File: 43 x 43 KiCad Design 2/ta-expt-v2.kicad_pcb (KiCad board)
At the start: 4 copper layers, 43 x 43 mm, 56 parts, among them IC1 BAR43SFILM, IC2 STS5PF30L, IC3 STM32L496VGT3, IC4 IS25LP128F-JBLA3, J1 Conn_01x05, J2 Conn_01x04, J3 USB_C_Receptacle_USB2.0, J4 Conn_01x05, J5 4-174639-8, J6 Conn_01x04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

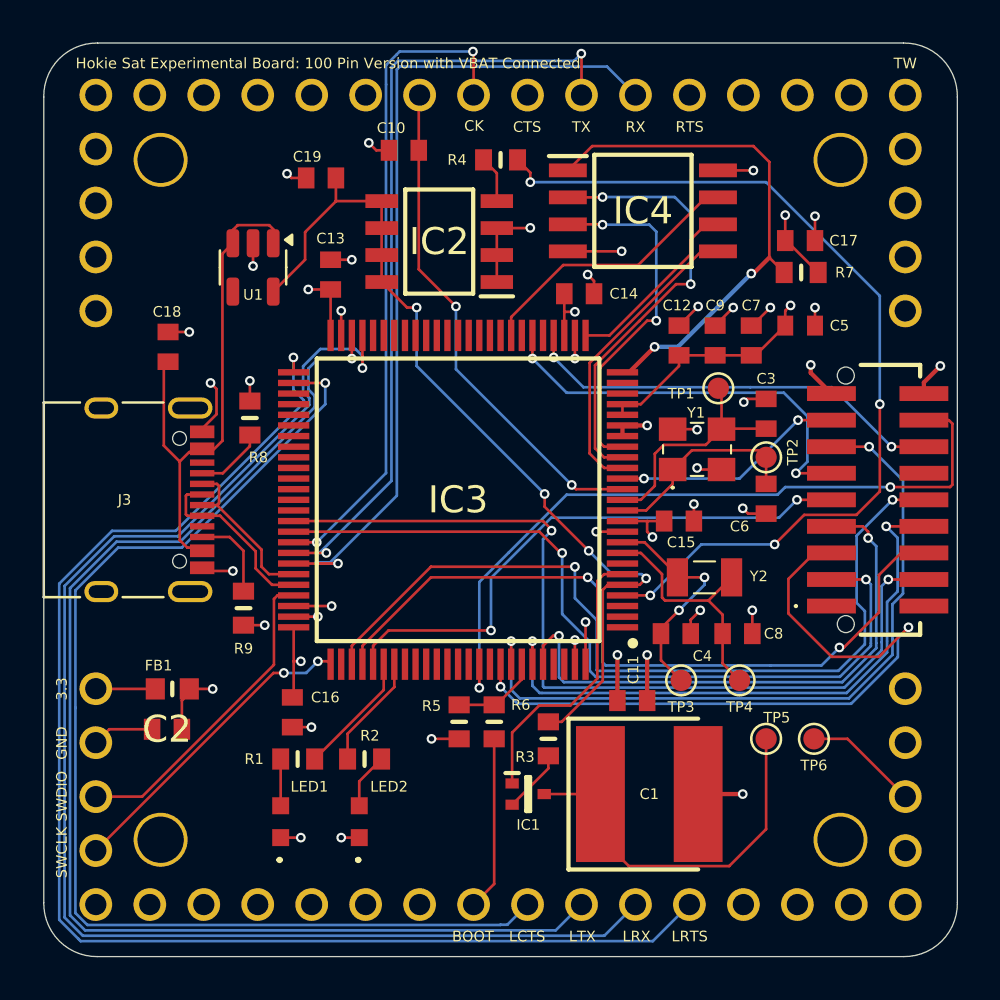
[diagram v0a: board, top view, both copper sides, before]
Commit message: Updating folder with everything that is needed, and also added in additional board with different design. Touched up some stuff too, but also need to add in datasheets and BOM
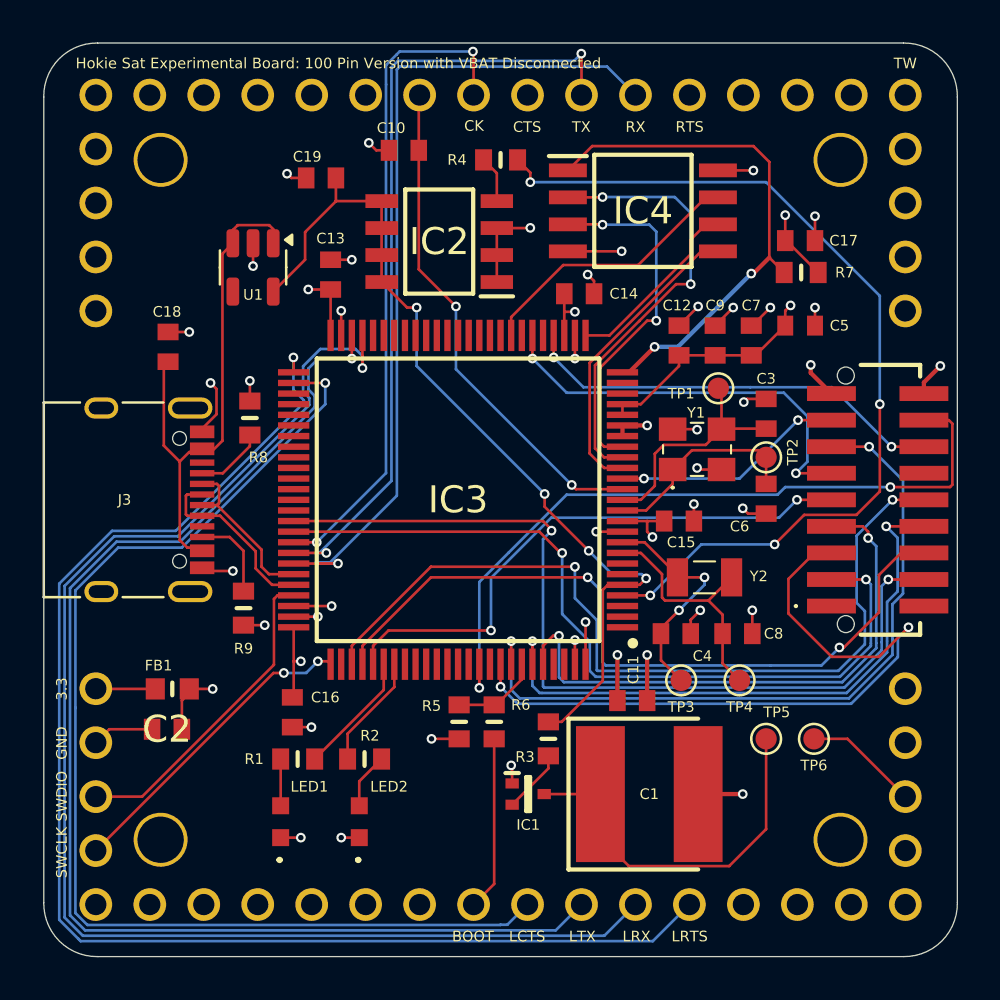
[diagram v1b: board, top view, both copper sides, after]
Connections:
- IC1 pad 1: /V_BAT -> /VDD_FILT
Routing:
- net /V_BAT: track 13.4 -> 0.00 mm
- net /VDD_FILT: track 43.2 -> 44.1 mm, vias 13 -> 14
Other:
- board text added: "Hokie Sat Experimental Board: 100 Pin Version with VBAT Disconnected"
- board text removed: "Hokie Sat Experimental Board: 100 Pin Version with VBAT Connected"
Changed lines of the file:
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@@
 			(drillshape 0)
 			(scaleselection 1)
-			(outputdirectory "Drill/")
+			(outputdirectory "Gerbers/")
 		)
 	)
@@
 		(tags "test point SMD pad")
 		(property "Reference" "TP5"
-			(at 0.5 -1 0)
+			(at 0.5 -1.25 0)
 			(layer "F.SilkS")
 			(effects
@@
 			(size 0.48 0.63)
 			(layers "F.Cu" "F.Paste" "F.Mask")
-			(net 12 "/V_BAT")
+			(net 3 "/VDD_FILT")
 			(pinfunction "A2")
 			(pintype "passive")
@@
 		)
 	)
-	(gr_text "Hokie Sat Experimental Board: 100 Pin Version with VBAT Connected"
+	(gr_text "Hokie Sat Experimental Board: 100 Pin Version with VBAT Disconnected"
 		(at 135 87.75 0)
 		(layer "F.SilkS")
@@
 	)
 	(segment
+		(start 155.545 121.35)
+		(end 155.545 120.545)
+		(width 0.127)
+		(layer "F.Cu")
+		(net 3)
+	)
+	(segment
 		(start 147 100.262)
 		(end 147 98.1)
@@
 	)
 	(segment
+		(start 155.545 120.545)
+		(end 155.5 120.5)
+		(width 0.127)
+		(layer "F.Cu")
+		(net 3)
+	)
+	(segment
 		(start 158 99.15)
 		(end 158 98.3)
@@
 	)
 	(via
+		(at 155.5 120.5)
+		(size 0.4572)
+		(drill 0.254)
+		(layers "F.Cu" "B.Cu")
+		(net 3)
+	)
+	(via
 		(at 156.4 95.2)
 		(size 0.4572)
@@
 	)
 	(segment
-		(start 156.816105 117.683895)
-		(end 155.545 118.955)
-		(width 0.127)
-		(layer "F.Cu")
-		(net 12)
-	)
-	(segment
-		(start 159.556 116.41179)
-		(end 158.283895 117.683895)
-		(width 0.127)
-		(layer "F.Cu")
-		(net 12)
-	)
-	(segment
-		(start 159.8735 111.5)
-		(end 159.556 111.8175)
-		(width 0.127)
-		(layer "F.Cu")
-		(net 12)
-	)
-	(segment
-		(start 158.283895 117.683895)
-		(end 156.816105 117.683895)
-		(width 0.127)
-		(layer "F.Cu")
-		(net 12)
-	)
-	(segment
-		(start 159.556 111.8175)
-		(end 159.556 116.41179)
-		(width 0.127)
-		(layer "F.Cu")
-		(net 12)
-	)
-	(segment
-		(start 160.738 111.5)
-		(end 159.8735 111.5)
-		(width 0.127)
-		(layer "F.Cu")
-		(net 12)
-	)
-	(segment
-		(start 155.545 118.955)
-		(end 155.545 121.35)
-		(width 0.127)
-		(layer "F.Cu")
-		(net 12)
-	)
-	(segment
